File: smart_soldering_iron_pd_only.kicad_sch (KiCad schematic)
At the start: 42 parts, among them J1 Conn_01x04_Pin, U3 ATMEGA328P-AU, Y1 16 MHZ

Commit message: added reset
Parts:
- added TP?: TestPoint, TestPoint:TestPoint_Pad_D1.5mm, symbol Connector:TestPoint
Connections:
- net at R14.2, U3.29 (PC6/~{RESET}): now also TP?.1
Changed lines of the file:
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@@
 	)
 	(junction
+		(at 73.66 80.01)
+		(diameter 0)
+		(color 0 0 0 0)
+	)
+	(junction
 		(at 58.42 134.62)
 		(diameter 0)
@@
 	(wire
 		(pts
+			(xy 73.66 80.01) (xy 85.09 80.01)
+		)
+		(stroke
+			(width 0)
+			(type default)
+		)
+	)
+	(wire
+		(pts
 			(xy 66.04 129.54) (xy 68.58 129.54)
 		)
@@
 	(wire
 		(pts
-			(xy 67.31 80.01) (xy 85.09 80.01)
+			(xy 67.31 80.01) (xy 73.66 80.01)
 		)
 		(stroke
@@
 					(unit 1)
 				)
+			)
+		)
+	)
+	(symbol
+		(lib_id "Connector:TestPoint")
+		(at 73.66 80.01 0)
+		(unit 1)
+		(exclude_from_sim no)
+		(in_bom yes)
+		(on_board yes)
+		(dnp no)
+		(property "Reference" "TP?"
+			(at 68.58 76.962 0)
+			(effects
+				(font
+					(size 1.27 1.27)
+				)
+				(justify left)
+			)
+		)
+		(property "Value" "TestPoint"
+			(at 68.326 74.422 0)
+			(effects
+				(font
+					(size 1.27 1.27)
+				)
+				(justify left)
+			)
+		)
+		(property "Footprint" "TestPoint:TestPoint_Pad_D1.5mm"
+			(at 78.74 80.01 0)
+			(effects
+				(font
+					(size 1.27 1.27)
+				)
+				(hide yes)
+			)
+		)
+		(property "Datasheet" "~"
+			(at 78.74 80.01 0)
+			(effects
+				(font
+					(size 1.27 1.27)
+				)
+				(hide yes)
+			)
+		)
+		(property "Description" "test point"
+			(at 73.66 80.01 0)
+			(effects
+				(font
+					(size 1.27 1.27)
+				)
+				(hide yes)
+			)
+		)
+		(pin "1"
+		)
+		(instances
+			(project "smart_soldering_iron_pd_only"
+				(path "/2df86fbf-058b-45fc-8204-866599907949"
+					(reference "TP?")
+					(unit 1)
+				)

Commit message: added name and version to the silk screen
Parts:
- removed Y1: 16 MHZ, smart_soldering_iron:16_mhz_OSC-SMD_4P-L3.2-W2.5-BL, symbol Device:Crystal
- added X1: 16MHz, smart_soldering_iron:16_mhz_OSC-SMD_4P-L3.2-W2.5-BL, symbol smart_soldering_iron:X322516MLB4SI
- gave numbers to parts that had none: 1
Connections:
- net GND: now also X1.2 (GND), X1.4 (GND)
- net XAL1: now also X1.3 (OSC2)
- net XAL2: now also X1.1 (OSC1)
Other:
- moved on the sheet: C4, C5

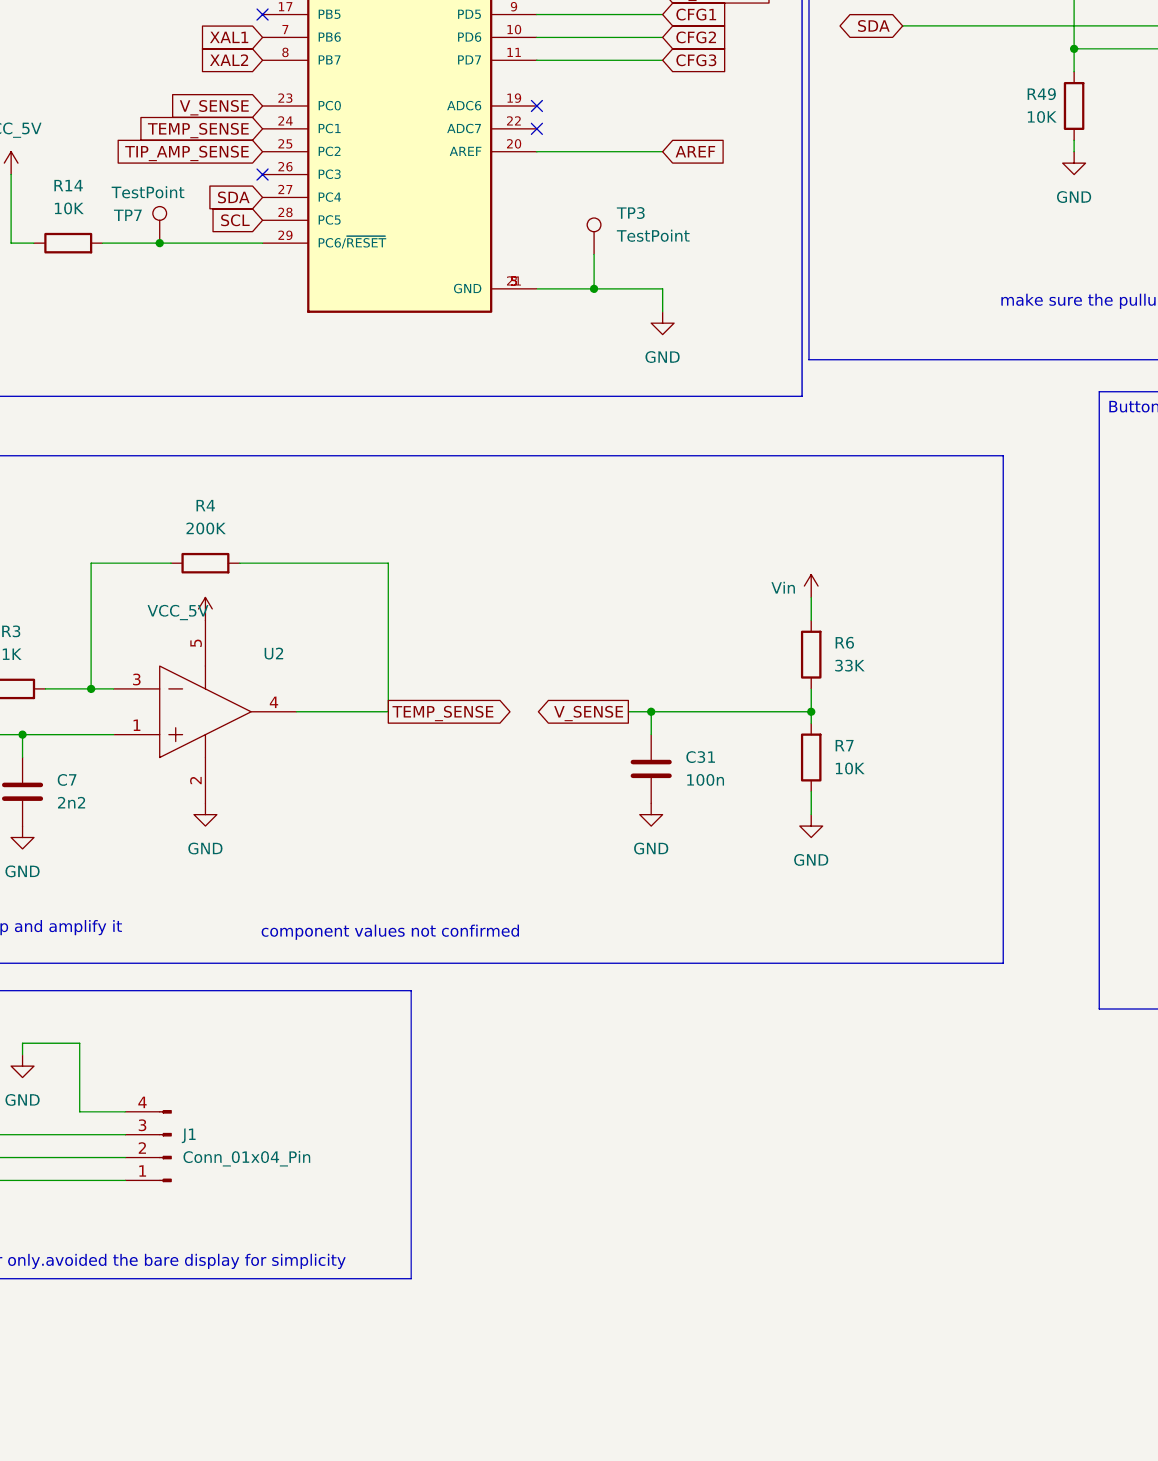
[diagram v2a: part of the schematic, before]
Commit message: error in tip dimension,added buzzer,increased length to 11cm
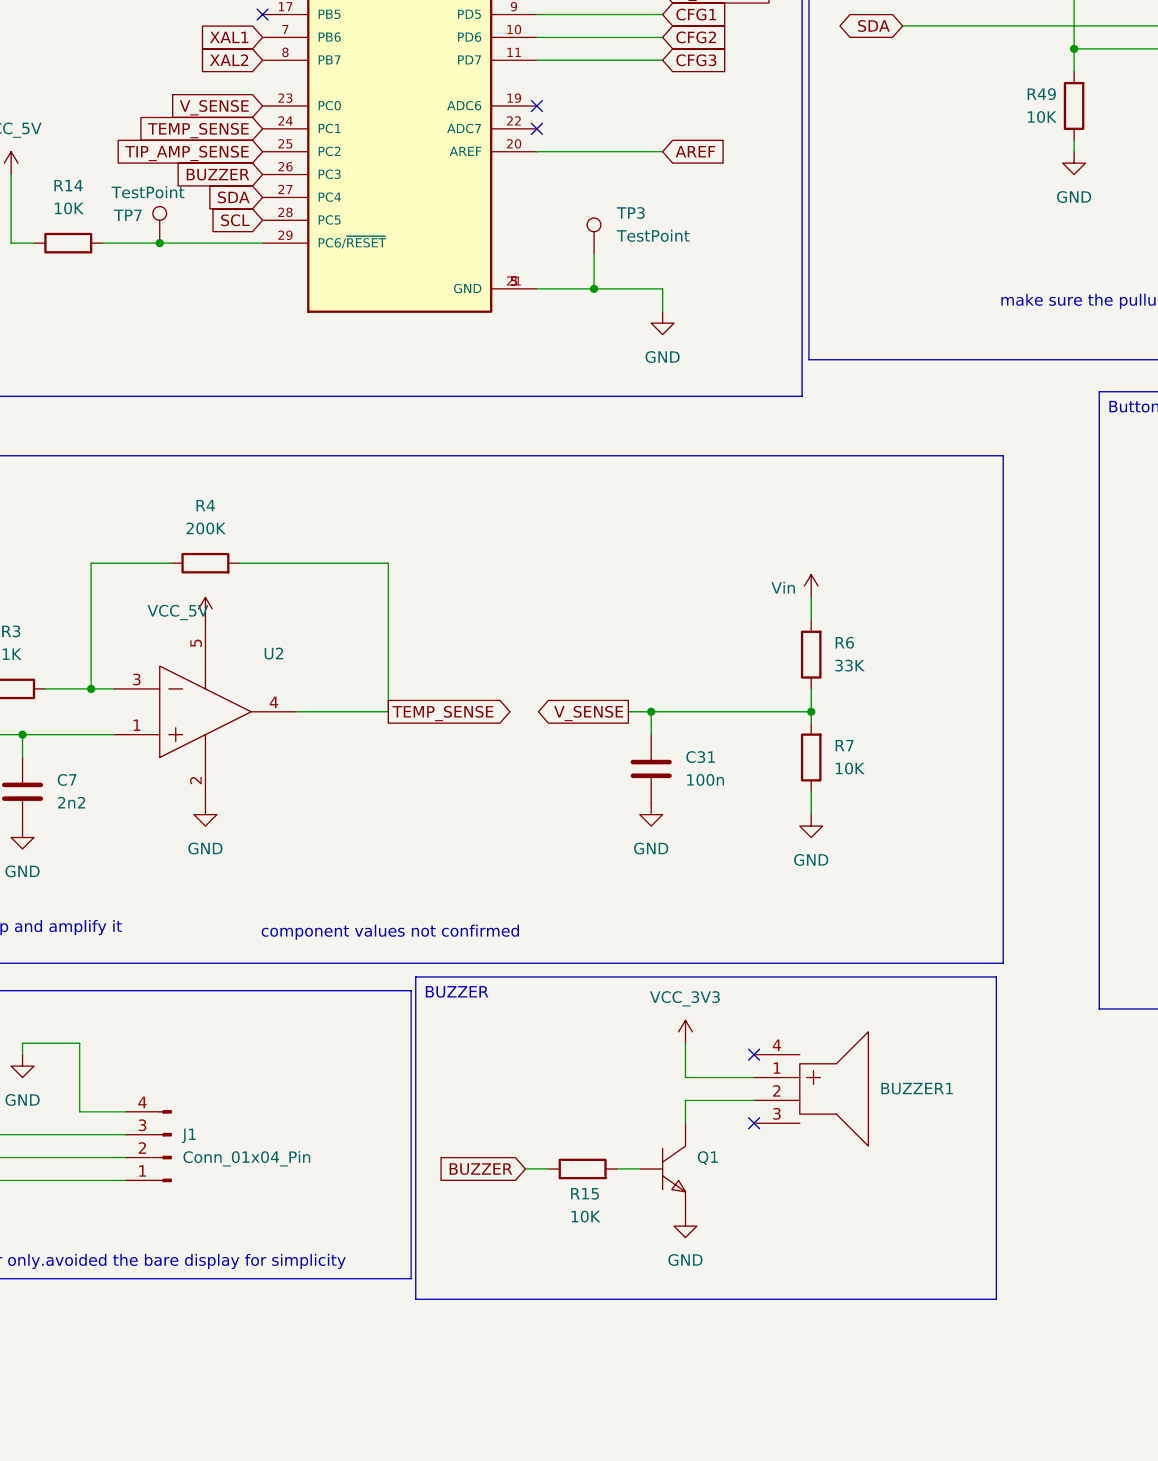
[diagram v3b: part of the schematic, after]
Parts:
- added BUZZER1: 2.7kHz, smart_soldering_iron:BUZZER_7525A_BUZ-SMD_4P-L7.5-W7.5-P7.59-TL, symbol smart_soldering_iron:MLT-7525
- added Q1: ~, smart_soldering_iron:S8050_TRANSIS_25V_0.5A_npn_SOT-23-3_L2.9-W1.3-P1.90-LS2.4-BR, symbol smart_soldering_iron:S8050
- added R15: 10K, Resistor_SMD:R_0603_1608Metric, symbol Device:R
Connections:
- net GND: now also Q1.2 (E)
- net VCC_3V3: now also BUZZER1.1 (+)
- net BUZZER: now reaches U3.26 (PC3)
- net BUZZER: now also R15.1
- new net: BUZZER1.2 (-), Q1.3 (C)
- new net: Q1.1 (B), R15.2
- no-connect marks 14 -> 15

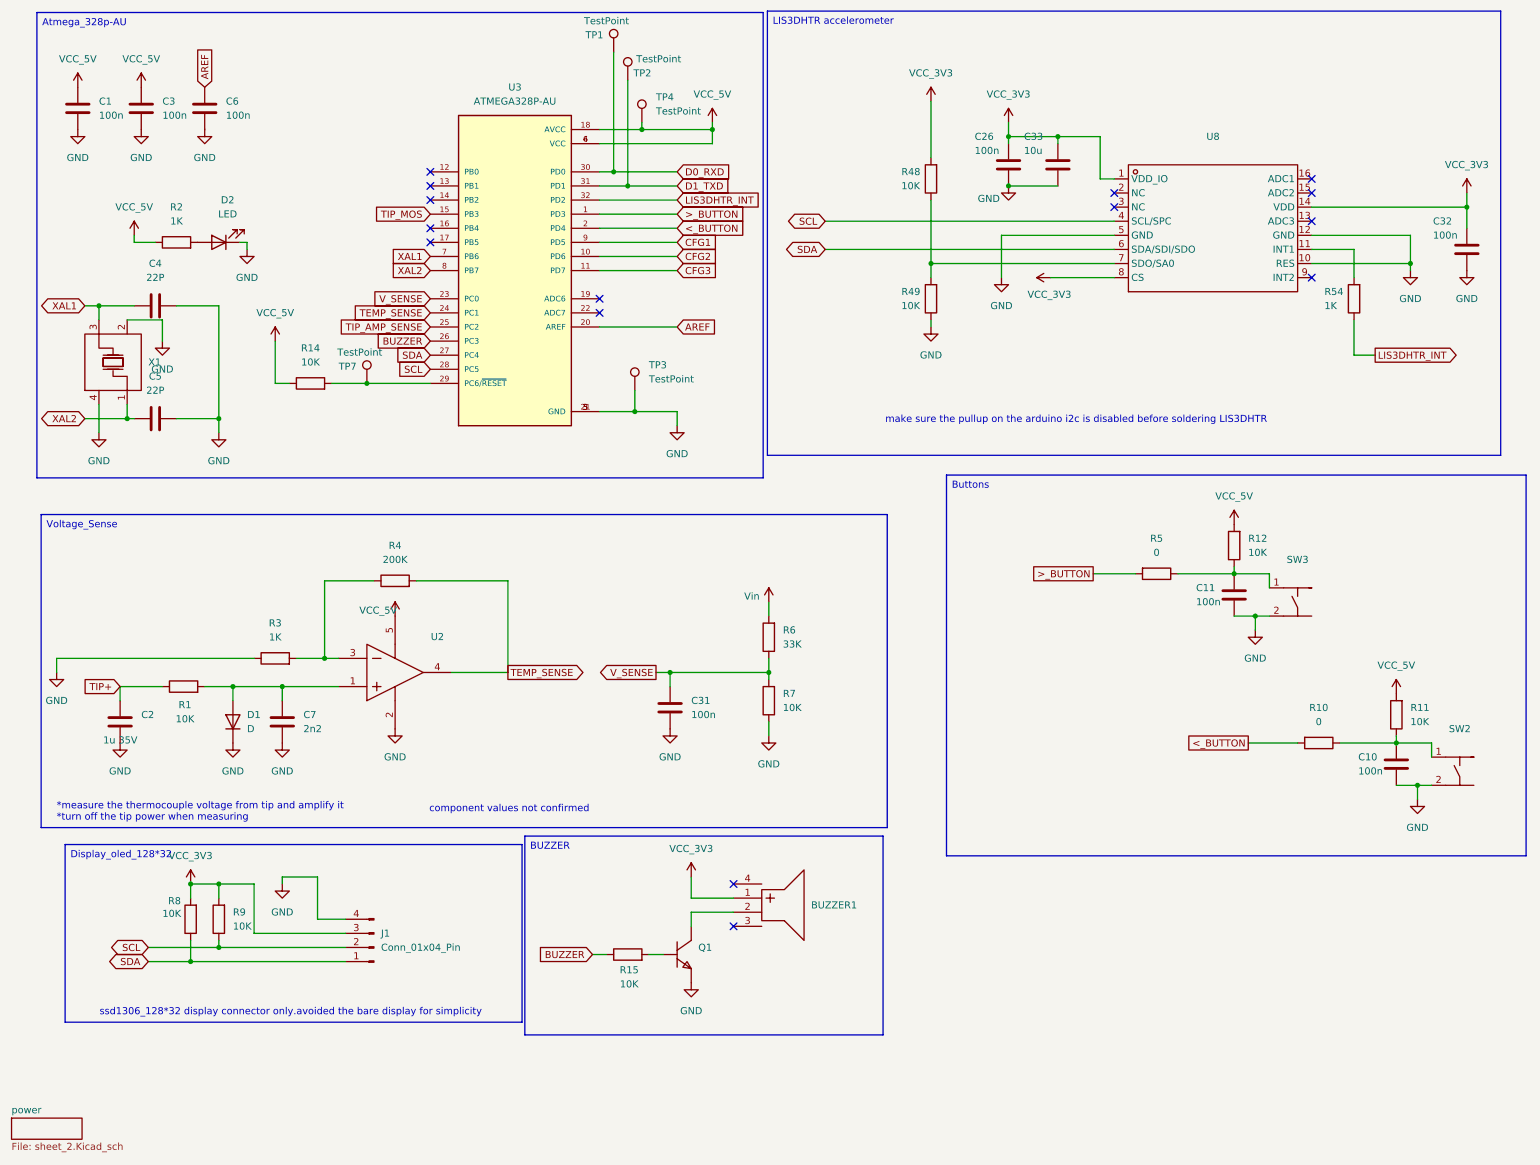
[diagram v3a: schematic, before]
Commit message: added rgb led
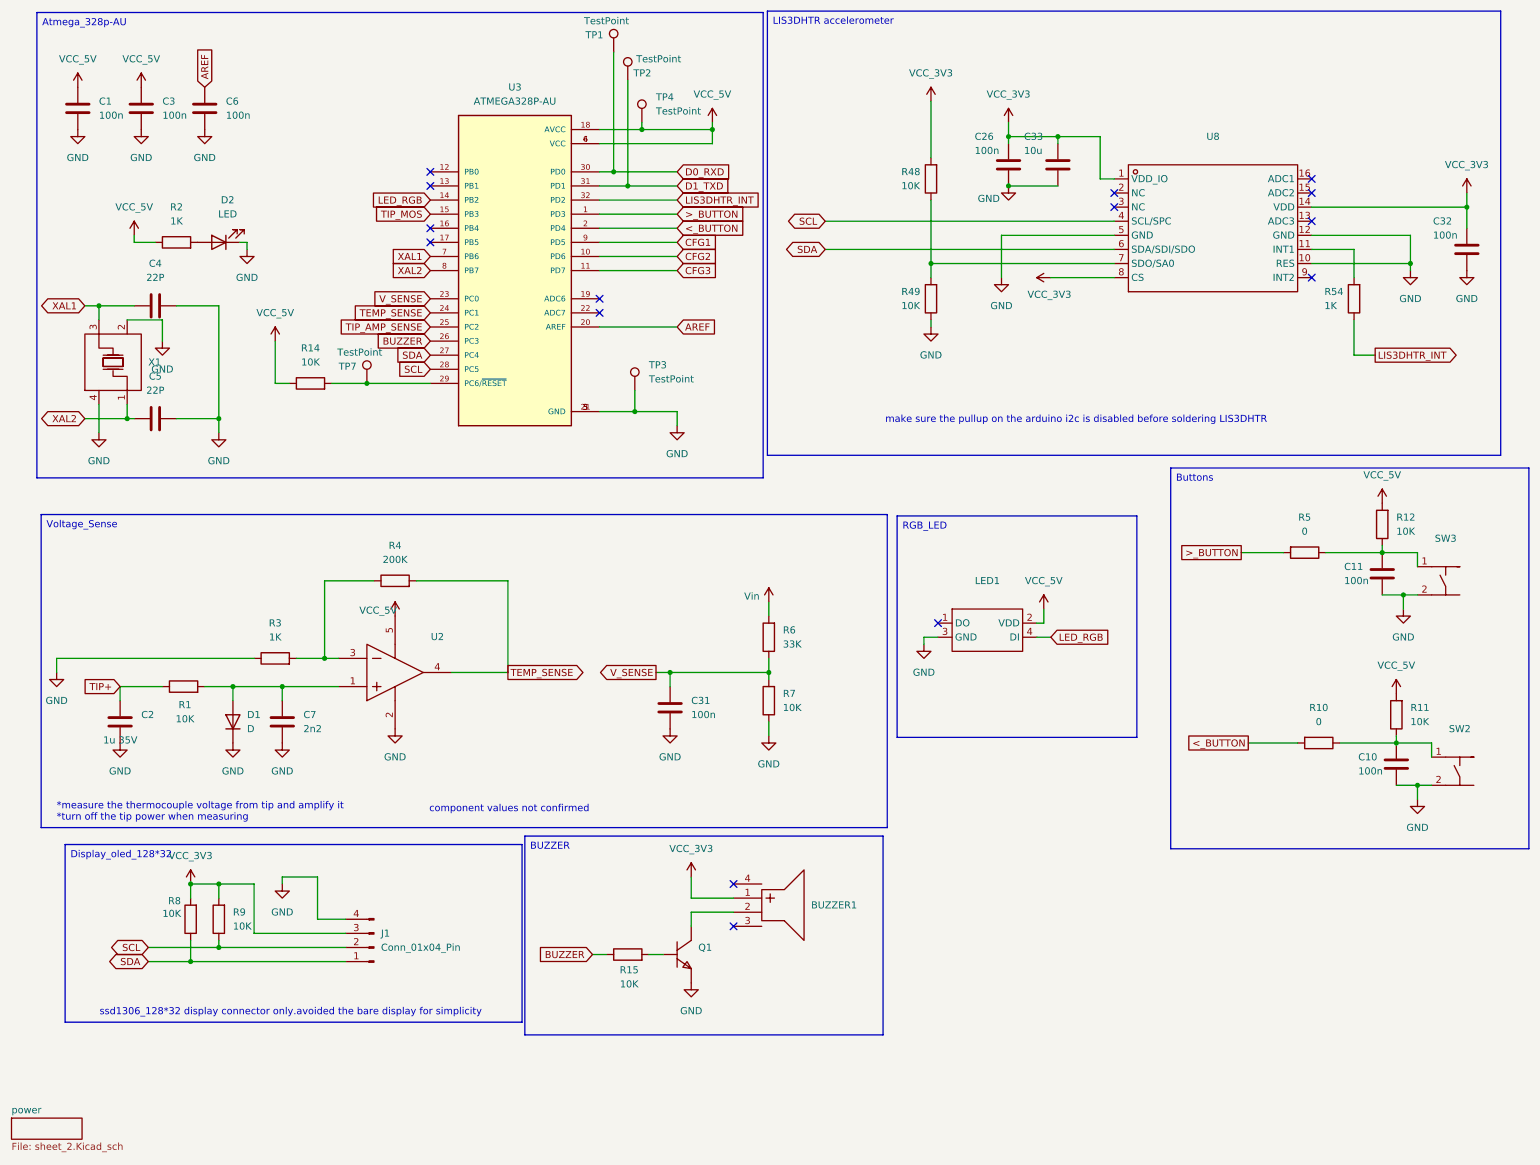
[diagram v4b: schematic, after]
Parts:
- added LED1: ~, smart_soldering_iron:LED-SMD_4P-L1.6-W1.5_XL-1615RGBC-WS2812B-S, symbol smart_soldering_iron:XL-1615RGBC-WS2812B-S
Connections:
- net GND: now also LED1.3 (GND)
- net VCC_5V: now also LED1.2 (VDD)
- net LED_RGB: now reaches U3.14 (PB2)
- net LED_RGB: now also LED1.4 (DI)
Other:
- moved on the sheet: C11, R12, R5, SW3
